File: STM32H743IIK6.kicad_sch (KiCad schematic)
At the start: 55 parts, among them J4 USB-C, SW1 SW_Push, SW2 SW_Push, SW3 SW_Push, SW4 SW_Push, U4 STM32H723ZGTx, U8 TLV75733PDBV, Y1 25MHz, Y2 32.768KHz

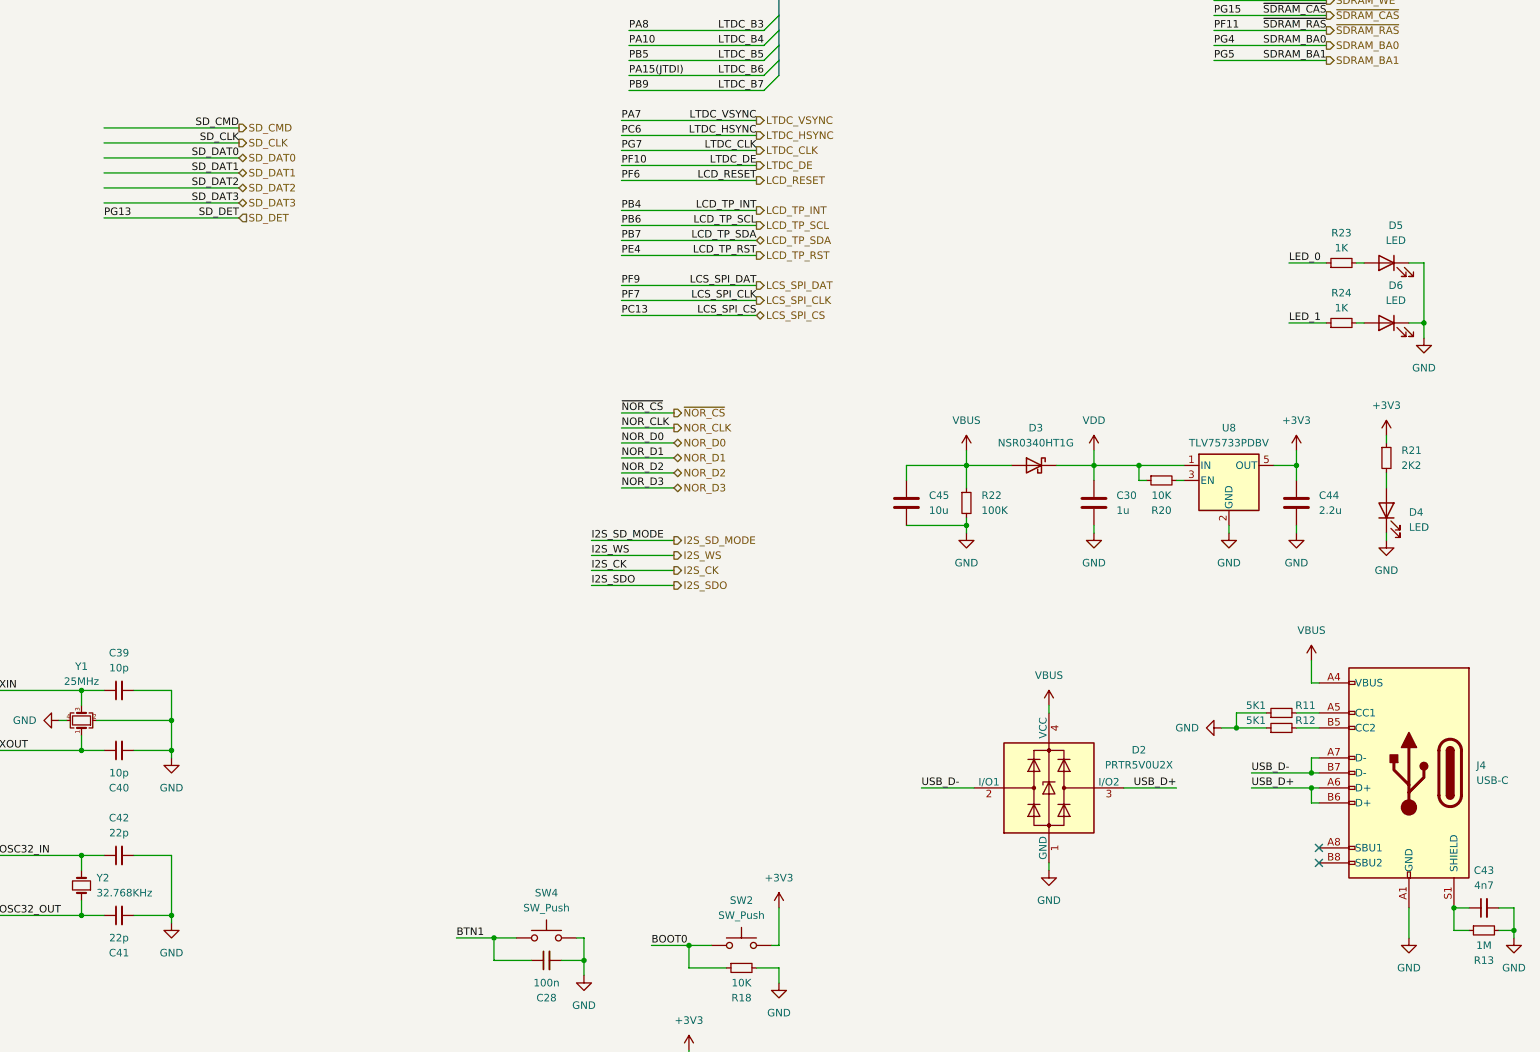
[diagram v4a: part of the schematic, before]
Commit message: Looks like FPC should be changed to XF2M-4015-1A
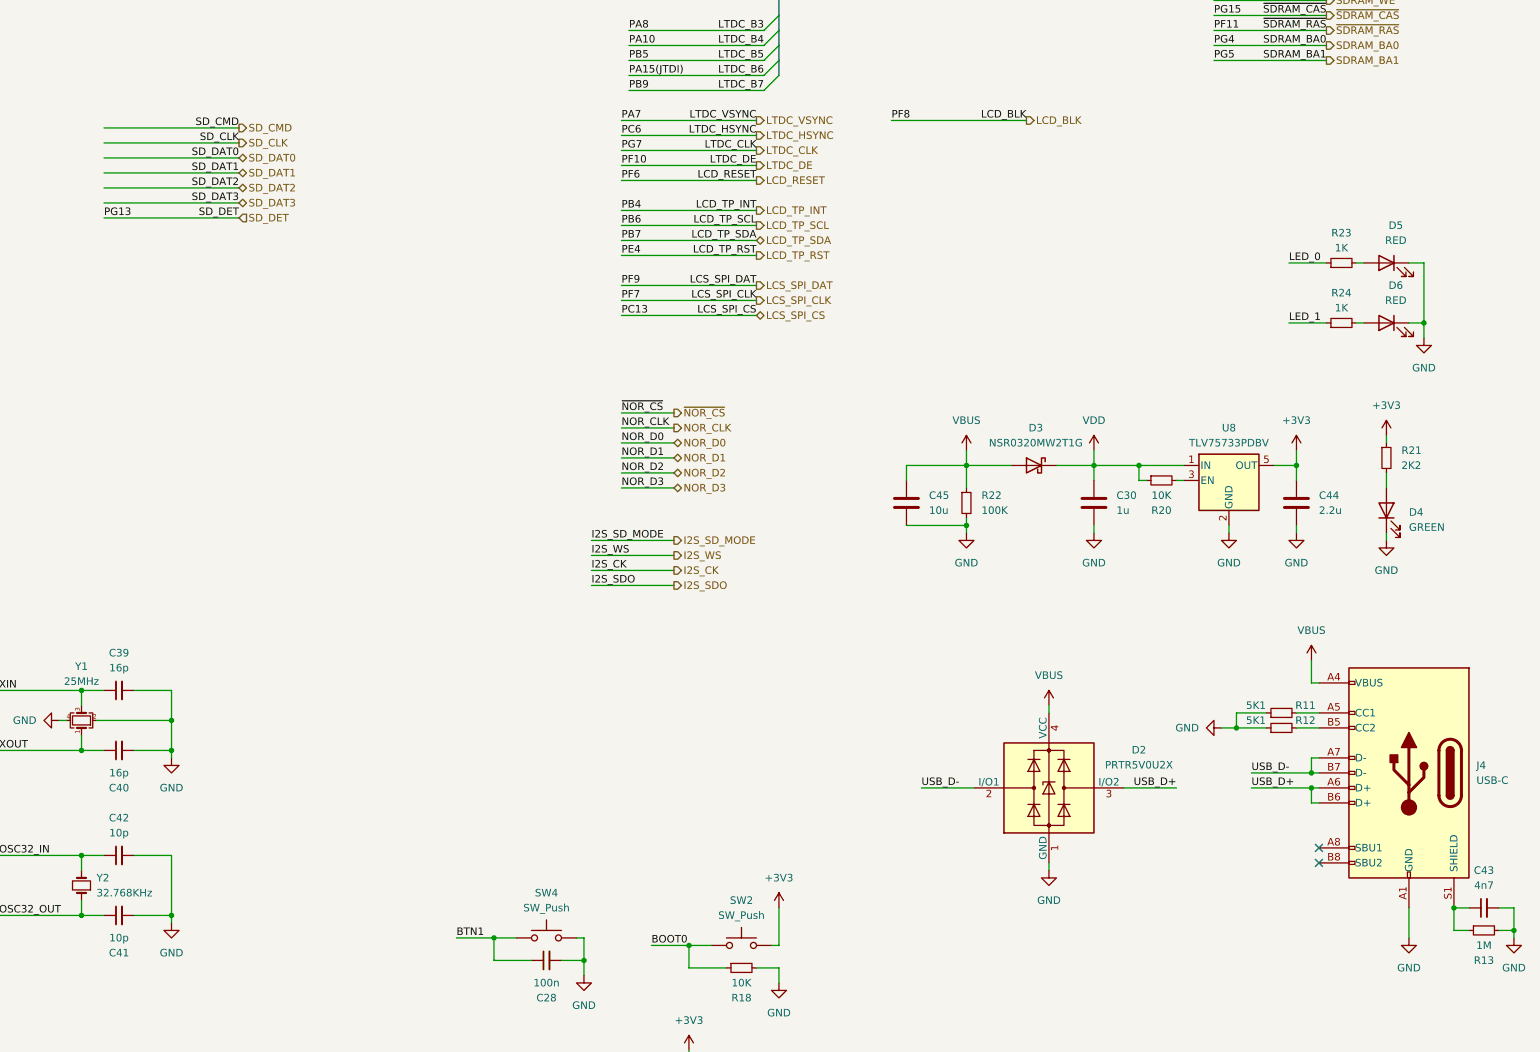
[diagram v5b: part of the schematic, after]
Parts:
- C10, C11, C12, C13, C14, C15, C16, C17, C24, C25, C27, C28, C4, C5, C6, C7, C8, C9: JLCPCB Part # (none) -> C307331
- C34, C35: JLCPCB Part # (none) -> C23630
- C39, C40: value 10p -> 16p; JLCPCB Part # (none) -> C77590
- C41, C42: value 22p -> 10p; JLCPCB Part # (none) -> C32949
- D2: JLCPCB Part # (none) -> C12333
- D3: value NSR0340HT1G -> NSR0320MW2T1G; JLCPCB Part # (none) -> C48192
- D4: value LED -> GREEN; JLCPCB Part # (none) -> C2297
- D5, D6: value LED -> RED; JLCPCB Part # (none) -> C84256
- J4: JLCPCB Part # (none) -> C963412
- R11, R12: JLCPCB Part # (none) -> C25905
- R17, R18, R19, R20: JLCPCB Part # (none) -> C25744
- R21: JLCPCB Part # (none) -> C25879
- R22: JLCPCB Part # (none) -> C25741
- R23, R24: JLCPCB Part # (none) -> C11702
- SW1, SW2, SW3, SW4: JLCPCB Part # (none) -> C127488
- U4: JLCPCB Part # (none) -> C730146
- U8: JLCPCB Part # (none) -> C485517
- Y1: JLCPCB Part # (none) -> C255954
- Y2: JLCPCB Part # (none) -> C99009
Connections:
- net PF8 renamed LCD_BLK

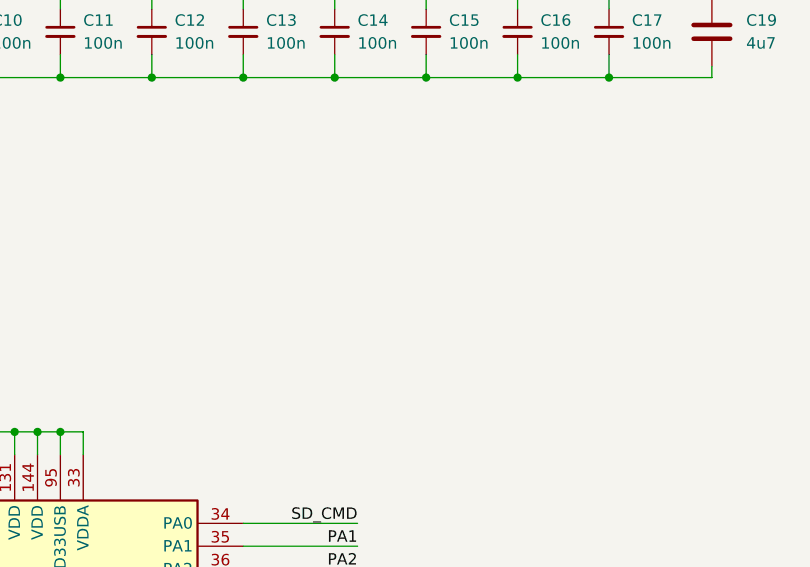
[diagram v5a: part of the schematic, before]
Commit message: Changed the FPC footprint and uart, added RTC battery connector
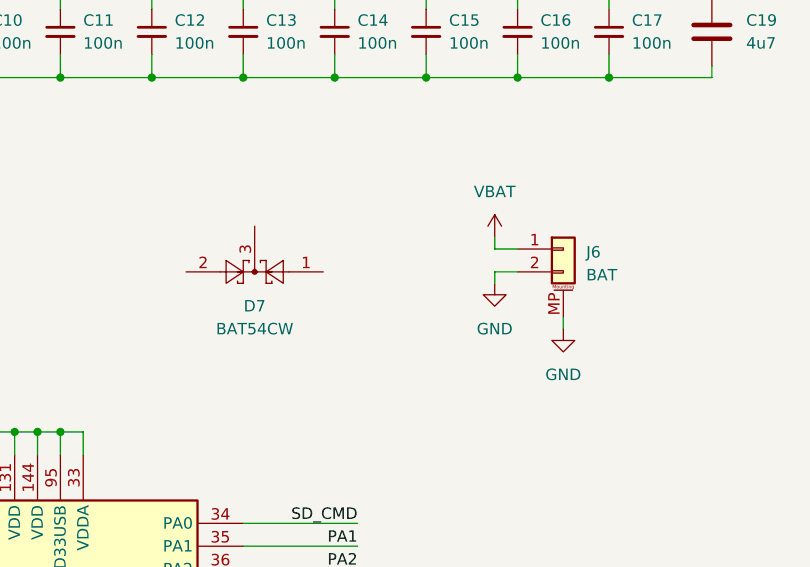
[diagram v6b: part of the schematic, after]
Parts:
- added D7: BAT54CW, Package_TO_SOT_SMD:SOT-323_SC-70, symbol Diode:BAT54CW
- added J6: BAT, Connector_Hirose:Hirose_DF13C_CL535-0402-2-51_1x02-1MP_P1.25mm_Vertical, symbol Connector_Generic_MountingPin:Conn_01x02_MountingPin
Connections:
- net GND: now also J6.2 (Pin_2), J6.MP (MountPin)
- new net VBAT: J6.1 (Pin_1)

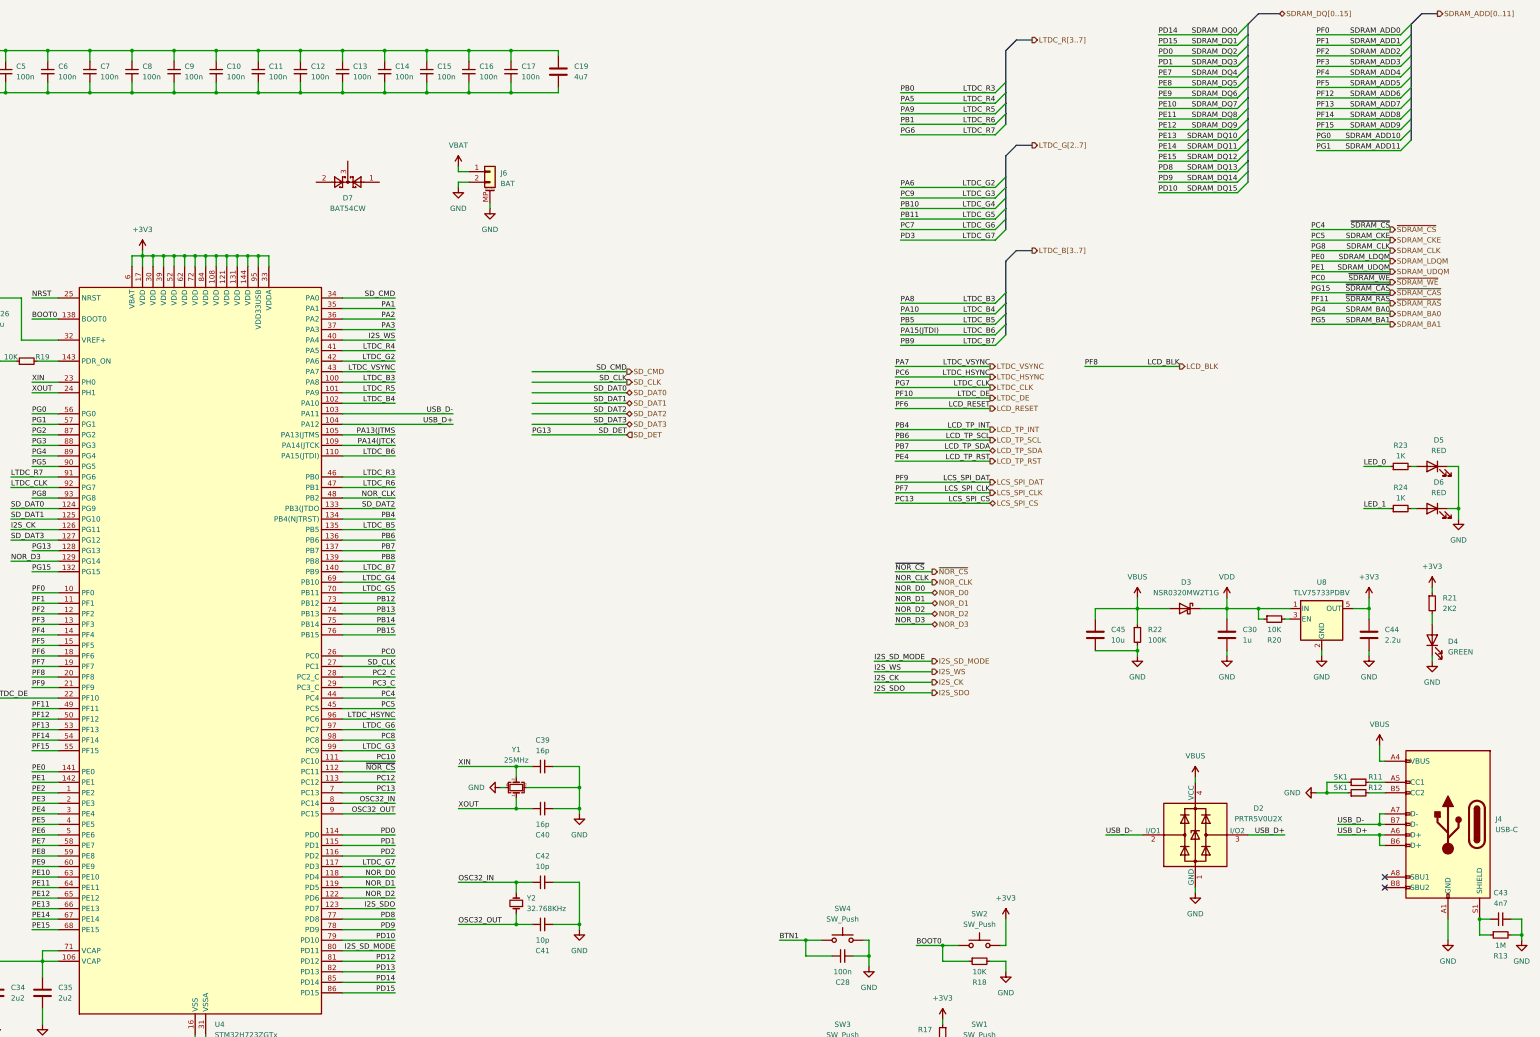
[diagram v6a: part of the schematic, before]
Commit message: Added UART esd
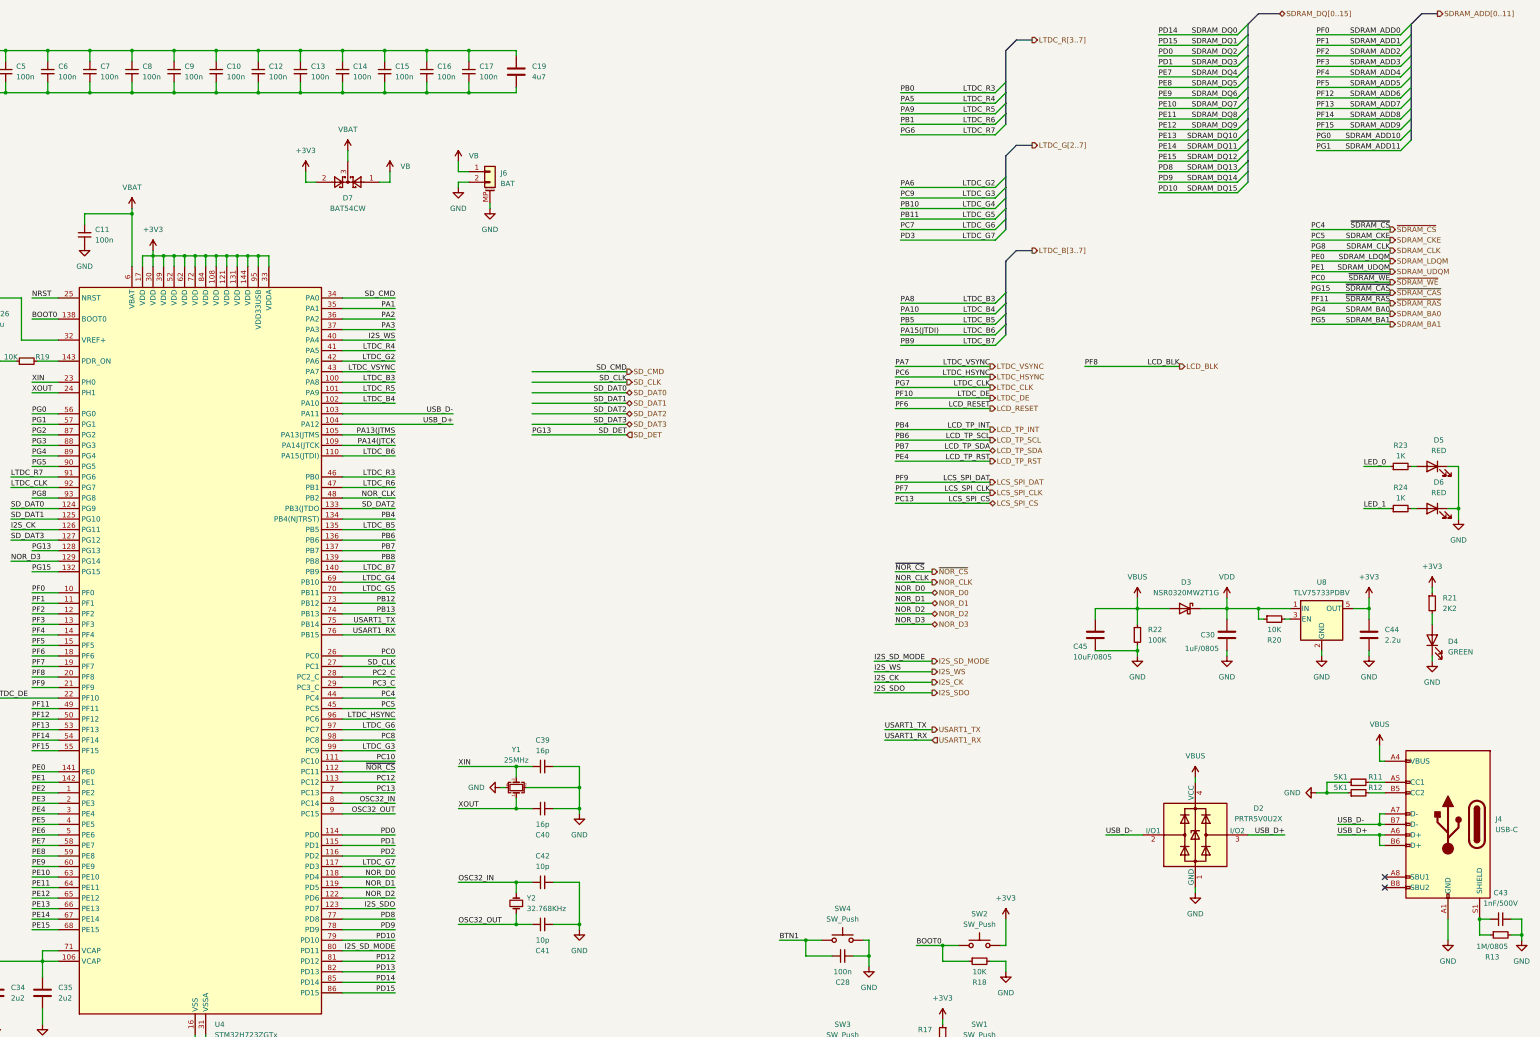
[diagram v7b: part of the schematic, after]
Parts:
- C19: JLCPCB Part # (none) -> C19666
- C26: JLCPCB Part # (none) -> C15849
- C30: value 1u -> 1uF/0805; JLCPCB Part # (none) -> C28323
- C43: value 4n7 -> 1nF/500V; footprint Capacitor_SMD:C_0402_1005Metric -> Capacitor_SMD:C_1206_3216Metric; JLCPCB Part # (none) -> C35216
- C44: JLCPCB Part # (none) -> C377773
- C45: value 10u -> 10uF/0805; JLCPCB Part # (none) -> C440198
- D7: JLCPCB Part # (none) -> C37704
- R13: value 1M -> 1M/0805; footprint Resistor_SMD:R_0402_1005Metric -> Resistor_SMD:R_0805_2012Metric; JLCPCB Part # (none) -> C17514
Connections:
- net +3V3: now also D7.2; no longer C11.1, U4.6 (VBAT)
- net VBAT: now also C11.1, D7.3, U4.6 (VBAT); no longer J6.1 (Pin_1)
- net VB: now reaches D7.1
- net VB: now also J6.1 (Pin_1)
- net PB14 renamed USART1_TX
- net PB15 renamed USART1_RX
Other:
- moved on the sheet: C11, C12, C13, C14, C15, C16, C17, C19
